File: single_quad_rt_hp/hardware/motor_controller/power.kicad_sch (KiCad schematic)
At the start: 8 parts, among them J201 Robot Power Bus

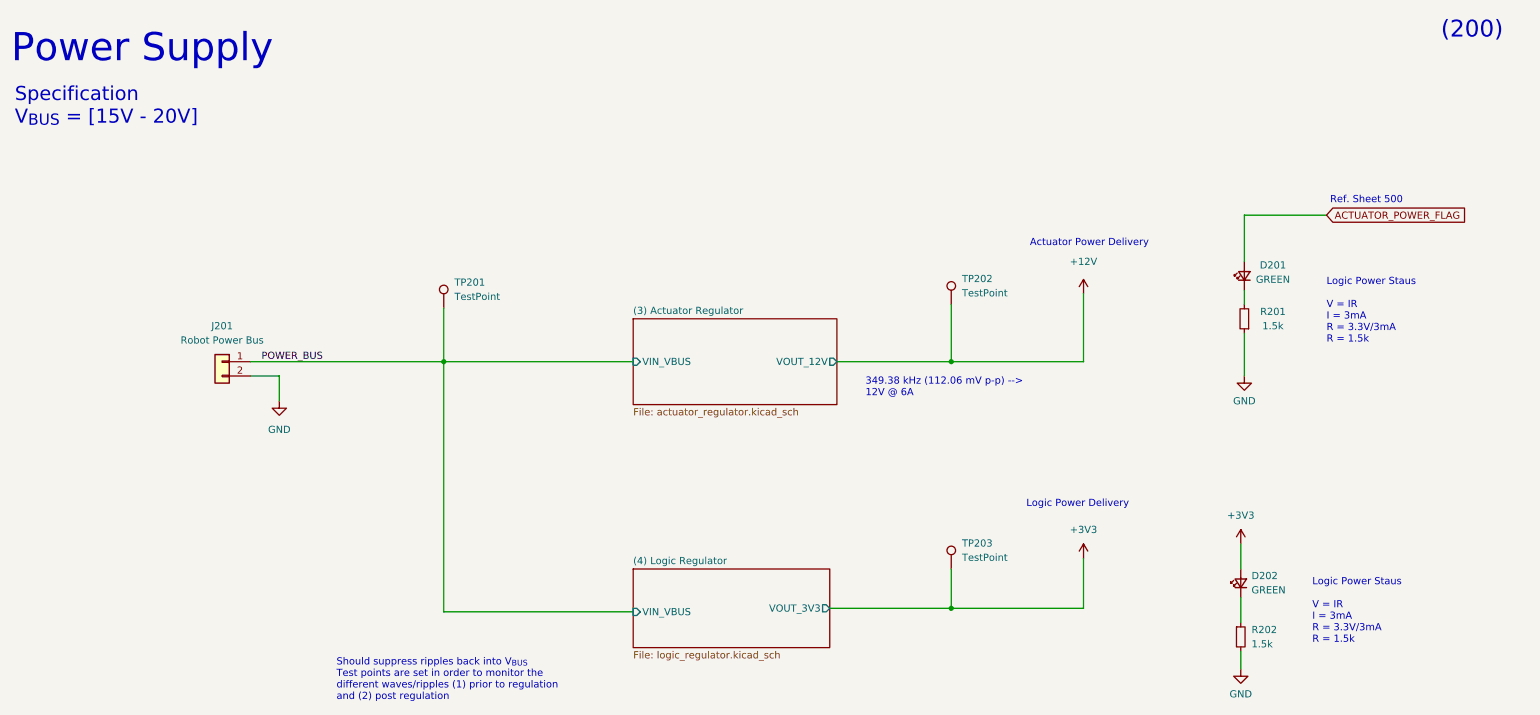
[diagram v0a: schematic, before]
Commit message: [single_quad_rt_hp] removing switching regs and simplifying the sceme
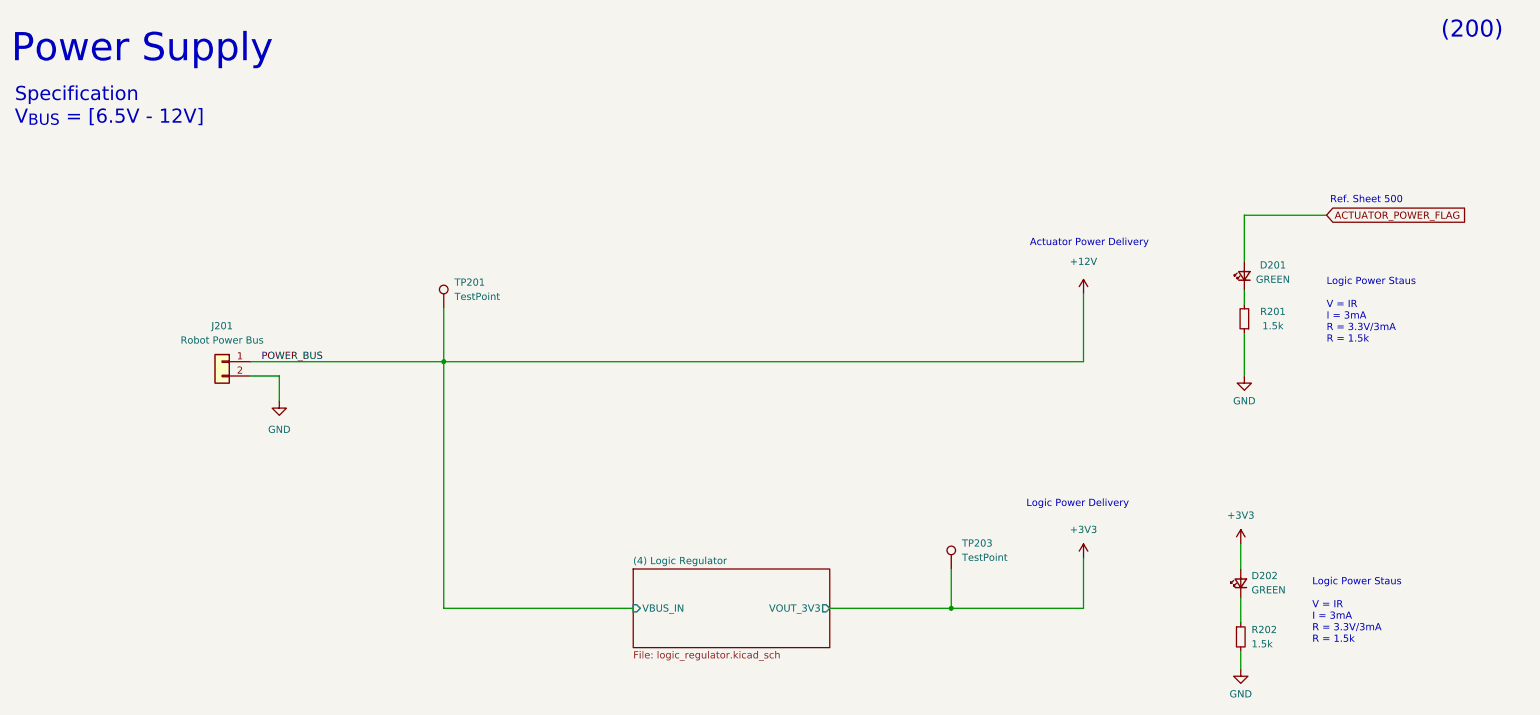
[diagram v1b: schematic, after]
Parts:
- removed TP202: TestPoint, TestPoint:TestPoint_Pad_1.5x1.5mm, symbol Connector:TestPoint
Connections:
- net POWER_BUS is gone; now on net +12V: J201.1 (Pin_1), TP201.1
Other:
- removed sheet (3) Actuator Regulator
- sheet (4) Logic Regulator ports: added VBUS_IN; removed VIN_VBUS
- note added: "Specification V_{BUS} = [6.5V - 12V]"
- note removed: "349.38 kHz (112.06 mV p-p) --> 12V @ 6A"
- note removed: "Should suppress ripples back into V_{BUS} Test points are set in order to monitor the different waves/ripples (1) prior to regulation and (2) post regulation"
- note removed: "Specification V_{BUS} = [15V - 20V]"
